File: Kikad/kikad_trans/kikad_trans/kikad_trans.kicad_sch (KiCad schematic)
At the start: 13 parts, among them J1 Conn_01x18_Pin, J3 Conn_01x18_Pin

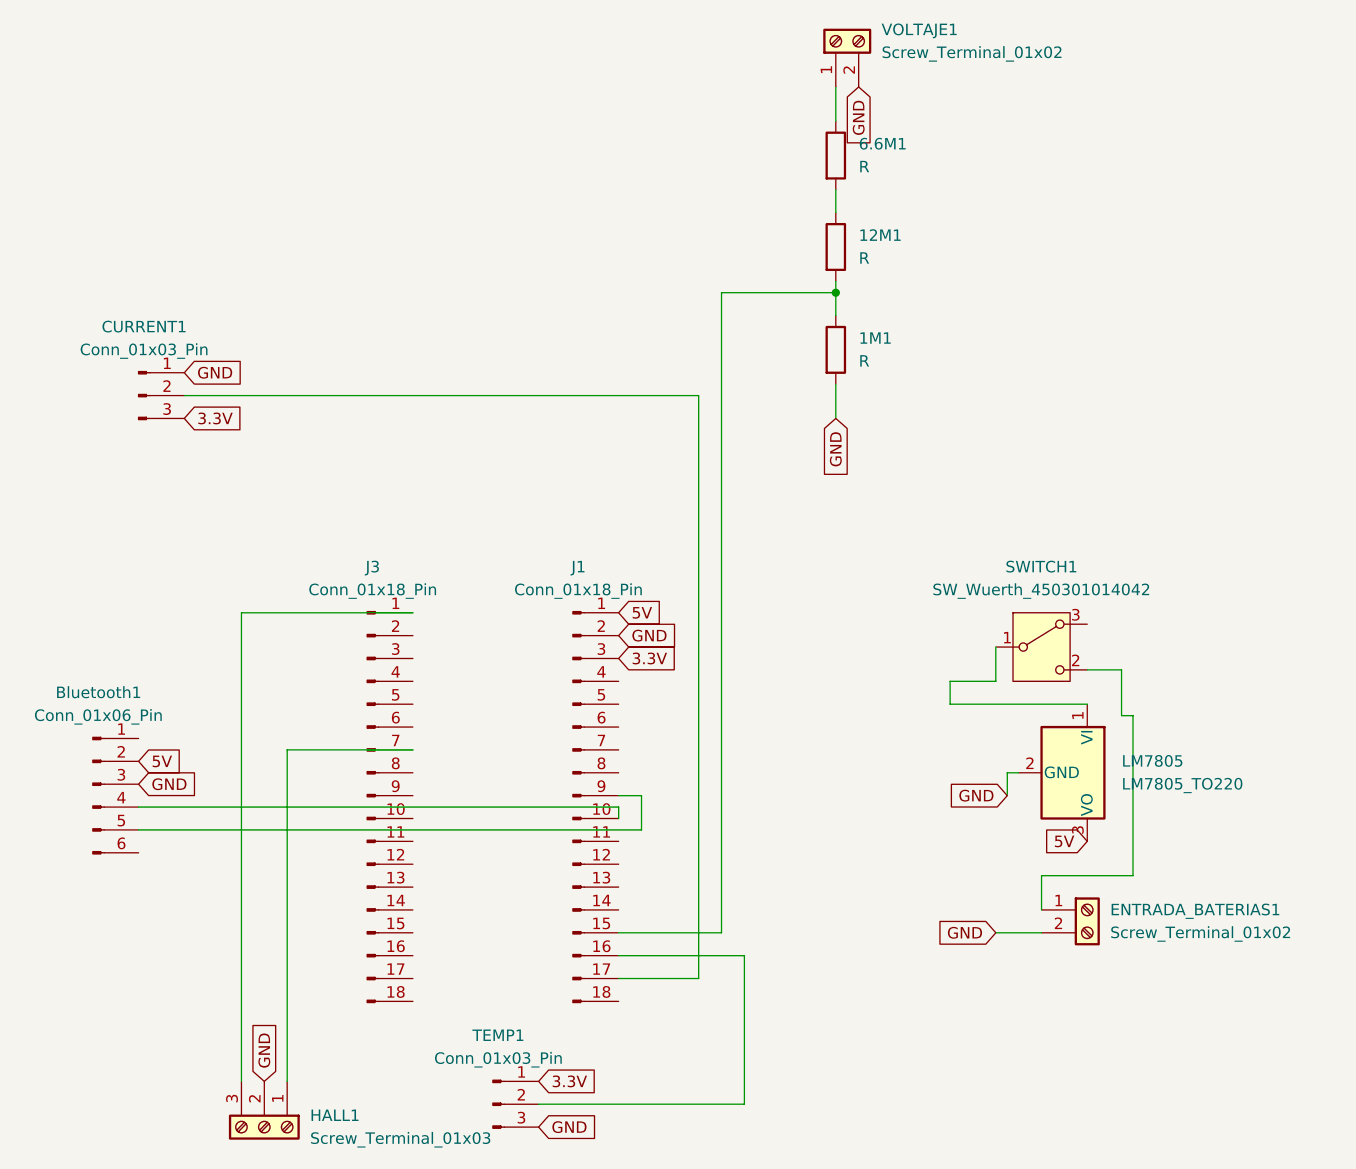
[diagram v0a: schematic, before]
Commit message: cambios en kikad y en codigo completo del sender
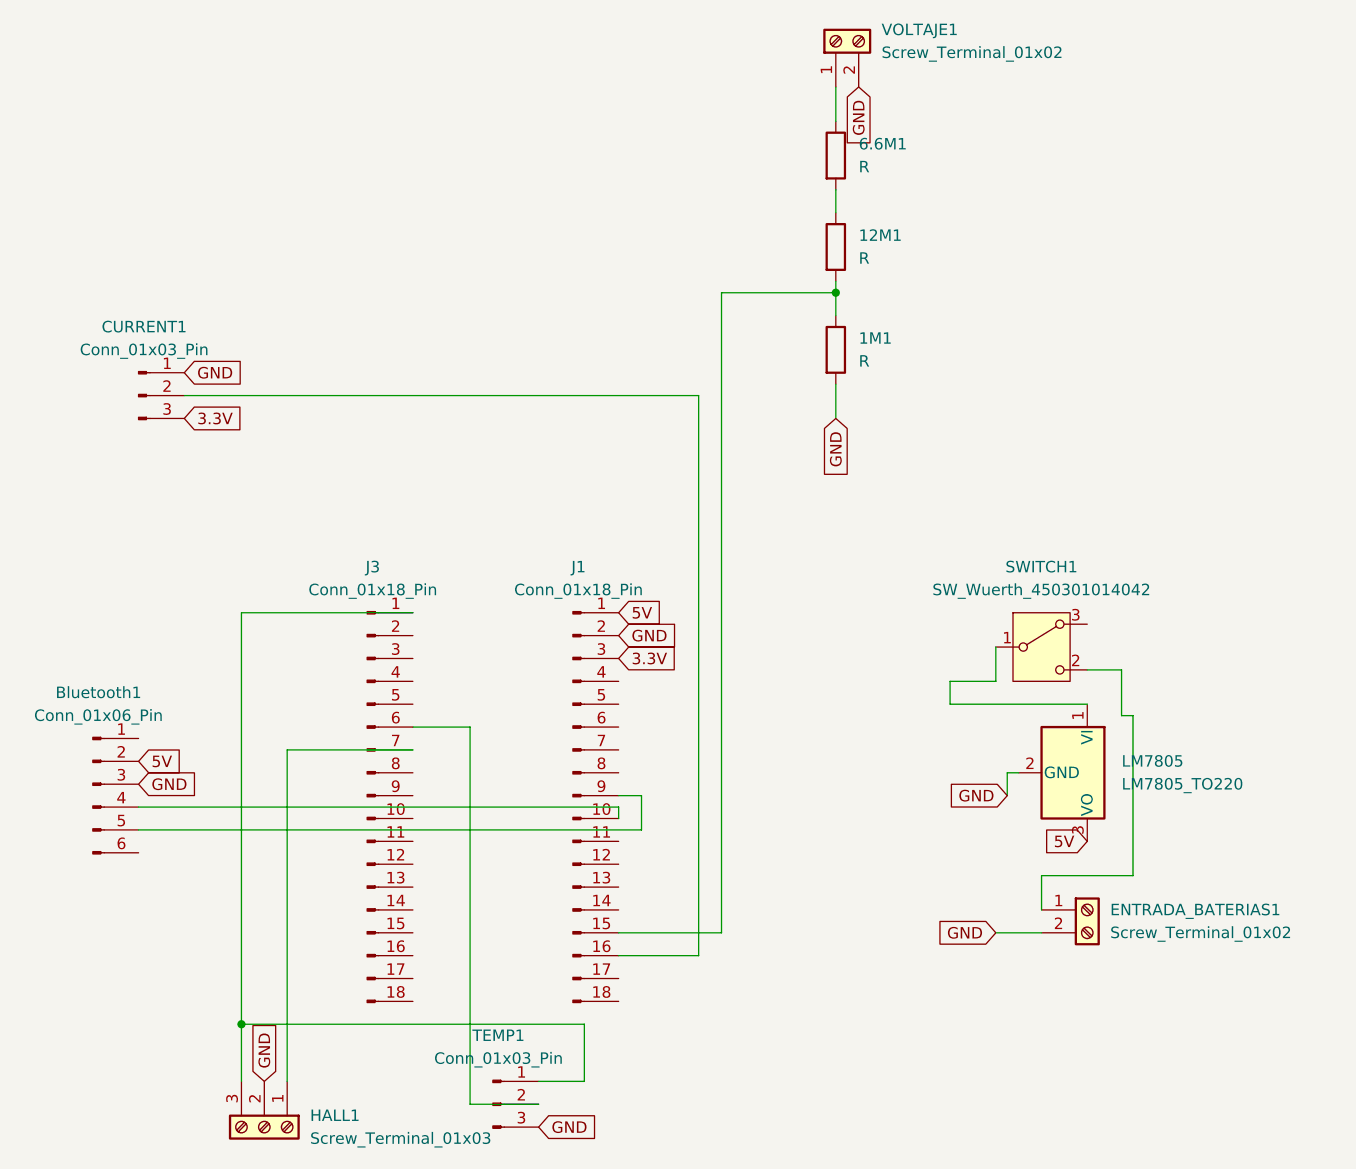
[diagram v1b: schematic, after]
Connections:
- net 3.3V: no longer TEMP1.1 (Pin_1)
- net at HALL1.3 (Pin_3), J3.1 (Pin_1): now also TEMP1.1 (Pin_1)
- net at J3.6 (Pin_6): now also TEMP1.2 (Pin_2)
- net at J1.16 (Pin_16): now also CURRENT1.2 (Pin_2); no longer TEMP1.2 (Pin_2)
- net at J1.17 (Pin_17): no longer CURRENT1.2 (Pin_2)
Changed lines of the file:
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@@
 		(color 0 0 0 0)
 	)
-	(wire
-		(pts
-			(xy 139.7 135.89) (xy 162.56 135.89)
-		)
-		(stroke
-			(width 0)
-			(type default)
-		)
+	(junction
+		(at 106.68 127)
+		(diameter 0)
+		(color 0 0 0 0)
 	)
 	(wire
@@
 	(wire
 		(pts
+			(xy 144.78 127) (xy 106.68 127)
+		)
+		(stroke
+			(width 0)
+			(type default)
+		)
+	)
+	(wire
+		(pts
 			(xy 111.76 96.52) (xy 125.73 96.52)
 		)
@@
 	(wire
 		(pts
+			(xy 125.73 93.98) (xy 132.08 93.98)
+		)
+		(stroke
+			(width 0)
+			(type default)
+		)
+	)
+	(wire
+		(pts
 			(xy 160.02 116.84) (xy 160.02 45.72)
 		)
@@
 	(wire
 		(pts
-			(xy 157.48 121.92) (xy 148.59 121.92)
+			(xy 106.68 127) (xy 106.68 133.35)
+		)
+		(stroke
+			(width 0)
+			(type default)
+		)
+	)
+	(wire
+		(pts
+			(xy 132.08 135.89) (xy 132.08 93.98)
 		)
 		(stroke
@@
 	(wire
 		(pts
+			(xy 144.78 133.35) (xy 144.78 127)
+		)
+		(stroke
+			(width 0)
+			(type default)
+		)
+	)
+	(wire
+		(pts
 			(xy 172.72 26.67) (xy 172.72 22.86)
 		)
@@
 	(wire
 		(pts
-			(xy 157.48 57.15) (xy 157.48 121.92)
-		)
-		(stroke
-			(width 0)
-			(type default)
-		)
-	)
-	(wire
-		(pts
-			(xy 162.56 135.89) (xy 162.56 119.38)
+			(xy 157.48 57.15) (xy 157.48 119.38)
 		)
 		(stroke
@@
 	(wire
 		(pts
-			(xy 106.68 133.35) (xy 106.68 81.28)
+			(xy 106.68 81.28) (xy 106.68 127)
 		)
 		(stroke
@@
 	(wire
 		(pts
+			(xy 148.59 119.38) (xy 157.48 119.38)
+		)
+		(stroke
+			(width 0)
+			(type default)
+		)
+	)
+	(wire
+		(pts
 			(xy 185.42 88.9) (xy 190.5 88.9)
 		)
@@
 	(wire
 		(pts
-			(xy 162.56 119.38) (xy 148.59 119.38)
+			(xy 139.7 135.89) (xy 132.08 135.89)
 		)
 		(stroke
@@
 		)
 	)
+	(wire
+		(pts
+			(xy 139.7 133.35) (xy 144.78 133.35)
+		)
+		(stroke
+			(width 0)
+			(type default)
+		)
+	)
 	(global_label "GND"
 		(shape input)
@@
 			(effects
 				(font
-					(size 1.27 1.27)
-				)
-				(justify left)
-				(hide yes)
-			)
-		)
-	)
-	(global_label "3.3V"
-		(shape input)
-		(at 139.7 133.35 0)
-		(fields_autoplaced yes)
-		(effects
-			(font
-				(size 1.27 1.27)
-			)
-			(justify left)
-		)
-		(property "Intersheetrefs" "${INTERSHEET_REFS}"
-			(at 146.7976 133.35 0)
-			(effects
-				(font

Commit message: Kikad ahora si
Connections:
- net GND: now also VOLTAJE1.1 (Pin_1); no longer VOLTAJE1.2 (Pin_2)
- net at 6.6M1.1: now also VOLTAJE1.2 (Pin_2); no longer VOLTAJE1.1 (Pin_1)
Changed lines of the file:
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@@
+	(wire
+		(pts
+			(xy 175.26 26.67) (xy 172.72 26.67)
+		)
+		(stroke
+			(width 0)
+			(type default)
+		)
+	)
 	(wire
 		(pts
@@
 	(wire
 		(pts
+			(xy 165.1 22.86) (xy 172.72 22.86)
+		)
+		(stroke
+			(width 0)
+			(type default)
+		)
+	)
+	(wire
+		(pts
 			(xy 106.68 81.28) (xy 125.73 81.28)
 		)
@@
 	(wire
 		(pts
-			(xy 172.72 26.67) (xy 172.72 22.86)
+			(xy 175.26 22.86) (xy 175.26 26.67)
 		)
 		(stroke
@@
 	(global_label "GND"
 		(shape input)
-		(at 175.26 22.86 270)
+		(at 165.1 22.86 270)
 		(fields_autoplaced yes)
 		(effects
@@
 		)
 		(property "Intersheetrefs" "${INTERSHEET_REFS}"
-			(at 175.26 29.6363 90)
+			(at 165.1 29.6363 90)
 			(effects
 				(font
